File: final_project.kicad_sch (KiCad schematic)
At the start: 20 parts, among them U1 ATmega328-P, U2 SGP30, U3 TXS0102DCT, U3_5V_to_1.8V_Voltage_Regulator ADP3336ARMZ, U4 LM2576HVT-5, Y1 16 MHz

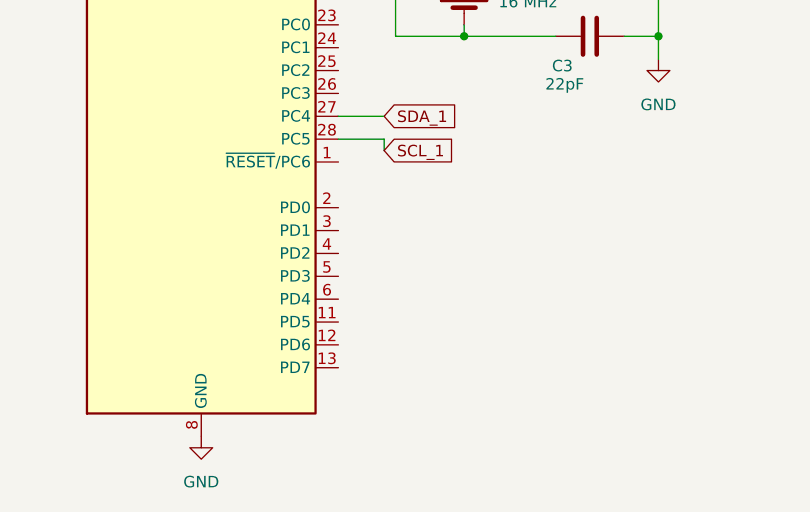
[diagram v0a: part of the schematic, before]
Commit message: Added USB Connections
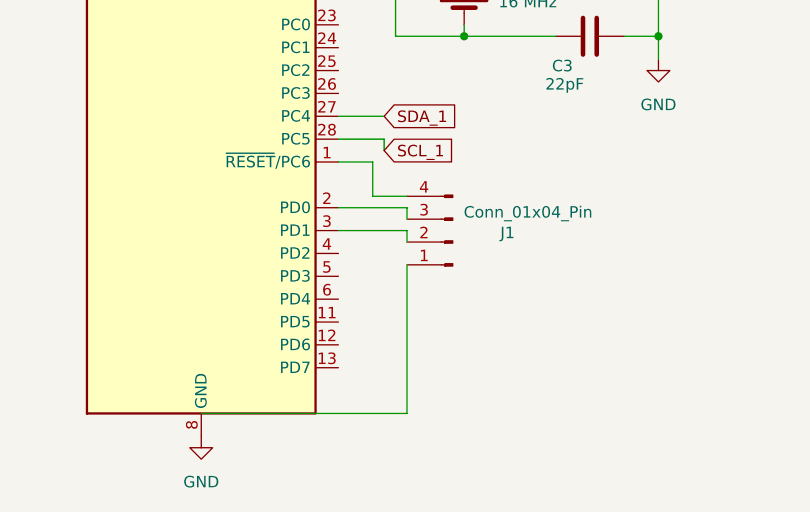
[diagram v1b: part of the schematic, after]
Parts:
- added J1: Conn_01x04_Pin, symbol Connector:Conn_01x04_Pin
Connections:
- net at U1.1 (~{RESET}/PC6): now also J1.4 (Pin_4)
- net at U1.2 (PD0): now also J1.3 (Pin_3)
- net at U1.3 (PD1): now also J1.2 (Pin_2)
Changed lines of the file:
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@@
+	(wire
+		(pts
+			(xy 87.63 173.99) (xy 110.49 173.99)
+		)
+		(stroke
+			(width 0)
+			(type default)
+		)
+	)
 	(wire
 		(pts
@@
 	(wire
 		(pts
+			(xy 106.68 149.86) (xy 110.49 149.86)
+		)
+		(stroke
+			(width 0)
+			(type default)
+		)
+	)
+	(wire
+		(pts
 			(xy 109.22 99.06) (xy 109.22 105.41)
 		)
@@
 	(wire
 		(pts
+			(xy 102.87 153.67) (xy 110.49 153.67)
+		)
+		(stroke
+			(width 0)
+			(type default)
+		)
+	)
+	(wire
+		(pts
+			(xy 110.49 173.99) (xy 110.49 157.48)
+		)
+		(stroke
+			(width 0)
+			(type default)
+		)
+	)
+	(wire
+		(pts
 			(xy 138.43 88.9) (xy 138.43 90.17)
 		)
@@
 	(wire
 		(pts
+			(xy 106.68 146.05) (xy 106.68 149.86)
+		)
+		(stroke
+			(width 0)
+			(type default)
+		)
+	)
+	(wire
+		(pts
 			(xy 187.96 128.27) (xy 195.58 128.27)
 		)
@@
 	(wire
 		(pts
+			(xy 110.49 151.13) (xy 110.49 152.4)
+		)
+		(stroke
+			(width 0)
+			(type default)
+		)
+	)
+	(wire
+		(pts
 			(xy 151.13 60.96) (xy 156.21 60.96)
 		)
@@
 	(wire
 		(pts
+			(xy 102.87 146.05) (xy 106.68 146.05)
+		)
+		(stroke
+			(width 0)
+			(type default)
+		)
+	)
+	(wire
+		(pts
 			(xy 95.25 85.09) (xy 95.25 88.9)
 		)
@@
 	(wire
 		(pts
+			(xy 102.87 151.13) (xy 110.49 151.13)
+		)
+		(stroke
+			(width 0)
+			(type default)
+		)
+	)
+	(wire
+		(pts
 			(xy 187.96 96.52) (xy 187.96 120.65)
 		)
@@
 		(pts
 			(xy 215.9 135.89) (xy 218.44 135.89)
+		)
+		(stroke
+			(width 0)
+			(type default)
+		)
+	)
+	(wire
+		(pts
+			(xy 110.49 153.67) (xy 110.49 154.94)
 		)
 		(stroke
@@
 					(unit 1)
 				)
+			)
+		)
+	)
+	(symbol
+		(lib_id "Connector:Conn_01x04_Pin")
+		(at 115.57 154.94 180)
+		(unit 1)
+		(exclude_from_sim no)
+		(in_bom yes)
+		(on_board yes)
+		(dnp no)
+		(property "Reference" "J1"
+			(at 121.666 153.924 0)
+			(effects
+				(font
+					(size 1.27 1.27)
+				)
+			)
+		)
+		(property "Value" "Conn_01x04_Pin"
+			(at 123.952 151.638 0)
+			(effects
+				(font
+					(size 1.27 1.27)
+				)
+			)
+		)
+		(property "Footprint" ""
+			(at 115.57 154.94 0)
+			(effects
+				(font
+					(size 1.27 1.27)
+				)
+				(hide yes)
+			)
+		)
+		(property "Datasheet" "~"
+			(at 115.57 154.94 0)
+			(effects
+				(font
+					(size 1.27 1.27)
+				)
+				(hide yes)
+			)
+		)
+		(property "Description" "Generic connector, single row, 01x04, script generated"
+			(at 115.57 154.94 0)
+			(effects
+				(font
+					(size 1.27 1.27)
+				)
+				(hide yes)
+			)
+		)
+		(pin "1"
+		)
+		(pin "2"
+		)
+		(pin "3"
+		)
+		(pin "4"
+		)
+		(instances
+			(project ""
+				(path "/69077819-e109-4340-8082-9c11186228b7"
+					(reference "J1")
+					(unit 1)
+				)

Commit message: Annotated Schematic
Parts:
- renumbered C2_In to C2_In1, C3_Out to C3_Out1, C4_NR to C4_NR1, R1_Pullup to R1_Pullup1, R2_Pullup to R2_Pullup1, U3_5V_to_1.8V_Voltage_Regulator to U3_5V_to_1.8V_Voltage_Regulator1
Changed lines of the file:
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@@
 		(on_board yes)
 		(dnp no)
-		(property "Reference" "C4_NR"
+		(property "Reference" "C4_NR1"
 			(at 121.666 94.234 90)
 			(effects
@@
 			(project ""
 				(path "/69077819-e109-4340-8082-9c11186228b7"
-					(reference "C4_NR")
+					(reference "C4_NR1")
 					(unit 1)
 				)
@@
 		(on_board yes)
 		(dnp no)
-		(property "Reference" "C3_Out"
+		(property "Reference" "C3_Out1"
 			(at 165.1 82.804 90)
 			(effects
@@
 			(project ""
 				(path "/69077819-e109-4340-8082-9c11186228b7"
-					(reference "C3_Out")
+					(reference "C3_Out1")
 					(unit 1)
 				)
@@
 		(on_board yes)
 		(dnp no)
-		(property "Reference" "C2_In"
+		(property "Reference" "C2_In1"
 			(at 91.948 91.44 0)
 			(effects
@@
 			(project ""
 				(path "/69077819-e109-4340-8082-9c11186228b7"
-					(reference "C2_In")
+					(reference "C2_In1")
 					(unit 1)
 				)
@@
 		(dnp no)
 		(fields_autoplaced yes)
-		(property "Reference" "R2_Pullup"
+		(property "Reference" "R2_Pullup1"
 			(at 173.99 121.9199 0)
 			(effects
@@
 			(project ""
 				(path "/69077819-e109-4340-8082-9c11186228b7"
-					(reference "R2_Pullup")
+					(reference "R2_Pullup1")
 					(unit 1)
 				)
@@
 		(dnp no)
 		(fields_autoplaced yes)
-		(property "Reference" "R1_Pullup"
+		(property "Reference" "R1_Pullup1"
 			(at 224.79 121.9199 0)
 			(effects
@@
 			(project ""
 				(path "/69077819-e109-4340-8082-9c11186228b7"
-					(reference "R1_Pullup")
+					(reference "R1_Pullup1")
 					(unit 1)
 				)
@@
 		(on_board yes)
 		(dnp no)
-		(property "Reference" "U3_5V_to_1.8V_Voltage_Regulator"
+		(property "Reference" "U3_5V_to_1.8V_Voltage_Regulator1"
 			(at 113.538 81.534 0)
 			(effects
@@
 			(project ""
 				(path "/69077819-e109-4340-8082-9c11186228b7"
-					(reference "U3_5V_to_1.8V_Voltage_Regulator")
-					(unit 1)
-				)
+					(reference "U3_5V_to_1.8V_Voltage_Regulator1")
+					(unit 1)
+				)

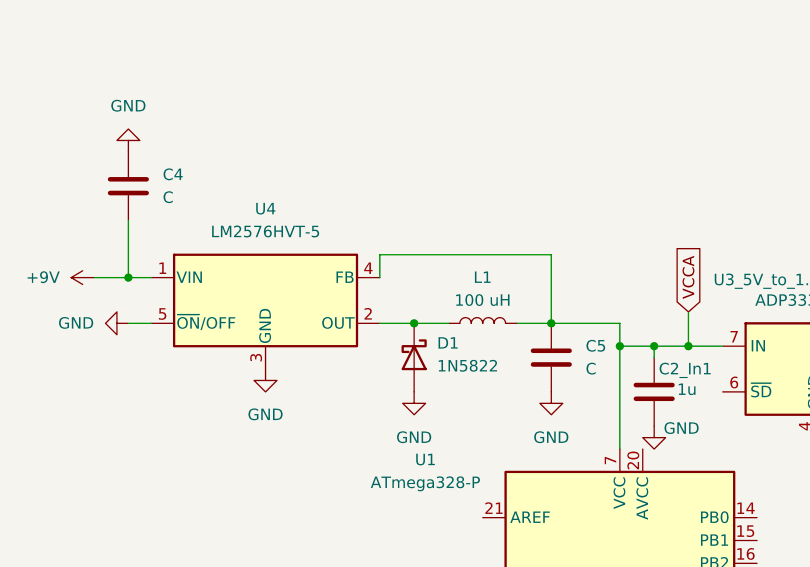
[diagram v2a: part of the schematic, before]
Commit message: Added Footprints
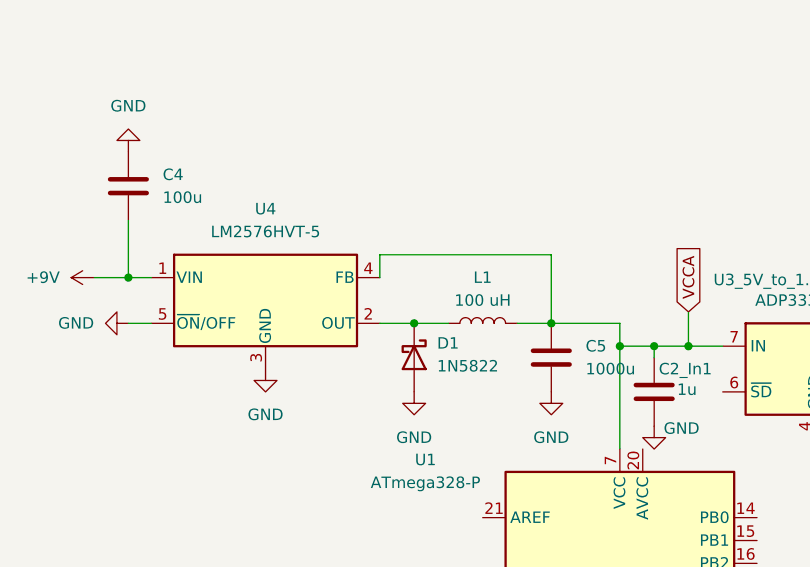
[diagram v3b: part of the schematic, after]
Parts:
- C1: footprint (none) -> GRM022D80G104ME15L:CAPC0402X22N
- C2, C3: footprint (none) -> footprints:CAPC17595_87N_KEM-M
- C2_In1, C3_Out1: footprint (none) -> C1u:CAP_CL10_SAM-M
- C4: value C -> 100u
- C5: value C -> 1000u
- R1: footprint (none) -> R76k8:YAG_MF25_YAG
- R1_Pullup1, R2_Pullup1: footprint (none) -> R10k:YAG_MF25_YAG
- R2: footprint (none) -> R147:YAG_MF25_YAG
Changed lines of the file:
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@@
 			)
 		)
-		(property "Value" "C"
+		(property "Value" "1000u"
 			(at 83.82 91.4399 0)
 			(effects
@@
 			)
 		)
-		(property "Footprint" ""
+		(property "Footprint" "C1u:CAP_CL10_SAM-M"
 			(at 168.91 87.9348 0)
 			(effects
@@
 			)
 		)
-		(property "Footprint" ""
+		(property "Footprint" "C1u:CAP_CL10_SAM-M"
 			(at 92.4052 97.79 0)
 			(effects
@@
 			)
 		)
-		(property "Value" "C"
+		(property "Value" "100u"
 			(at 36.83 72.3899 0)
 			(effects
@@
 			)
 		)
-		(property "Footprint" ""
+		(property "Footprint" "GRM022D80G104ME15L:CAPC0402X22N"
 			(at 188.9252 128.27 0)
 			(effects
@@
 			)
 		)
-		(property "Footprint" ""
+		(property "Footprint" "R147:YAG_MF25_YAG"
 			(at 136.652 101.6 90)
 			(effects
@@
 			)
 		)
-		(property "Footprint" ""
+		(property "Footprint" "R10k:YAG_MF25_YAG"
 			(at 169.672 123.19 90)
 			(effects
@@
 			)
 		)
-		(property "Footprint" ""
+		(property "Footprint" "R10k:YAG_MF25_YAG"
 			(at 220.472 123.19 90)
 			(effects
@@
 			)
 		)
-		(property "Footprint" ""
+		(property "Footprint" "R76k8:YAG_MF25_YAG"
 			(at 140.208 93.98 90)
 			(effects
@@
 			)
 		)
-		(property "Footprint" ""
+		(property "Footprint" "footprints:CAPC17595_87N_KEM-M"
 			(at 134.62 122.2248 0)
 			(effects
@@
 			)
 		)
-		(property "Footprint" ""
+		(property "Footprint" "footprints:CAPC17595_87N_KEM-M"
 			(at 127 133.0452 0)
 			(effects

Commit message: Added C100uF
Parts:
- C4: footprint (none) -> c100u:CAP_GRM31_1206_MUR-M
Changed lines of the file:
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@@
 			)
 		)
-		(property "Footprint" ""
+		(property "Footprint" "c100u:CAP_GRM31_1206_MUR-M"
 			(at 33.9852 74.93 0)
 			(effects

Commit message: Added Capacitor Library
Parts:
- C4_NR1: footprint (none) -> C10nF:G-155_MUR
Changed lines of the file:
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@@
 			)
 		)
-		(property "Footprint" ""
+		(property "Footprint" "C10nF:G-155_MUR"
 			(at 126.0348 90.17 0)
 			(effects

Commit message: Added Inductor Library
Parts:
- J1: footprint (none) -> Connector_PinHeader_1.00mm:PinHeader_1x04_P1.00mm_Vertical
- L1: footprint (none) -> Inductor100uH:IND_TAIYO_BRL3225_TAY
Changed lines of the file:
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@@
 			)
 		)
-		(property "Footprint" ""
+		(property "Footprint" "Connector_PinHeader_1.00mm:PinHeader_1x04_P1.00mm_Vertical"
 			(at 115.57 154.94 0)
 			(effects
@@
 			)
 		)
-		(property "Footprint" ""
+		(property "Footprint" "Inductor100uH:IND_TAIYO_BRL3225_TAY"
 			(at 72.39 86.36 0)
 			(effects

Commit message: Added Crystal Footprint Library
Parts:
- Y1: footprint (none) -> ECS_160_20_5PX_TR:XTAL_ECS-160-20-5PX-TR
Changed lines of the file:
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@@
 			)
 		)
-		(property "Footprint" ""
+		(property "Footprint" "ECS_160_20_5PX_TR:XTAL_ECS-160-20-5PX-TR"
 			(at 116.84 127 0)
 			(effects

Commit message: Footprint Library Completed
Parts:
- C5: footprint (none) -> 1000uF:CAP_YX_10X16_RUB
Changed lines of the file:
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@@
 			)
 		)
-		(property "Footprint" ""
+		(property "Footprint" "1000uF:CAP_YX_10X16_RUB"
 			(at 80.9752 93.98 0)
 			(effects
